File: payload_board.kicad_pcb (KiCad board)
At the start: 4 copper layers, 100 x 100 mm, 100 parts, among them IC1 RP2040_QFN56, IC2 AZ1117CH-3.3TRG1, J1 Cam_PicoLock, J12 5025700893, J12 FC Breakout, J15 SWC, J2 Cam_Conn, J3 Antenna_Conn, J4 usb jumper, J5 Display_Conn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

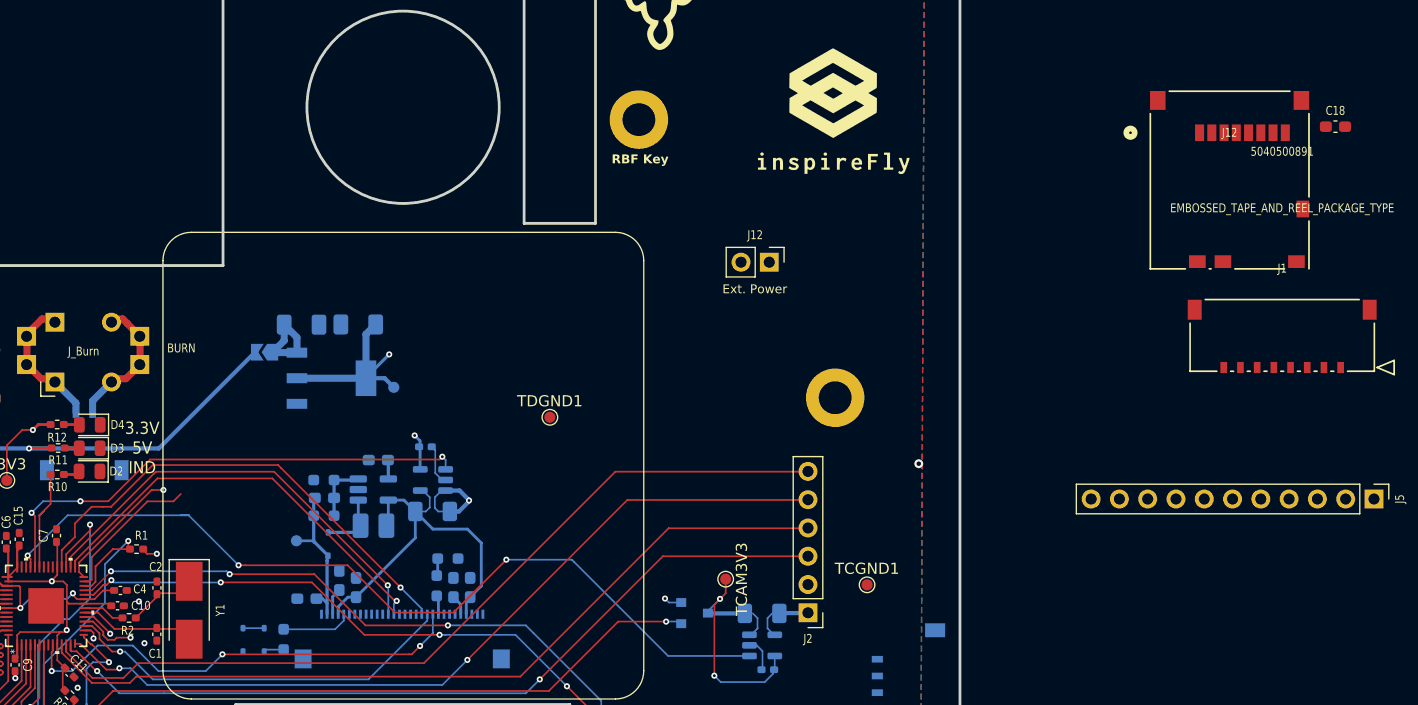
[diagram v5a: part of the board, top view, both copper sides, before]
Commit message: Moved the sd card on the board
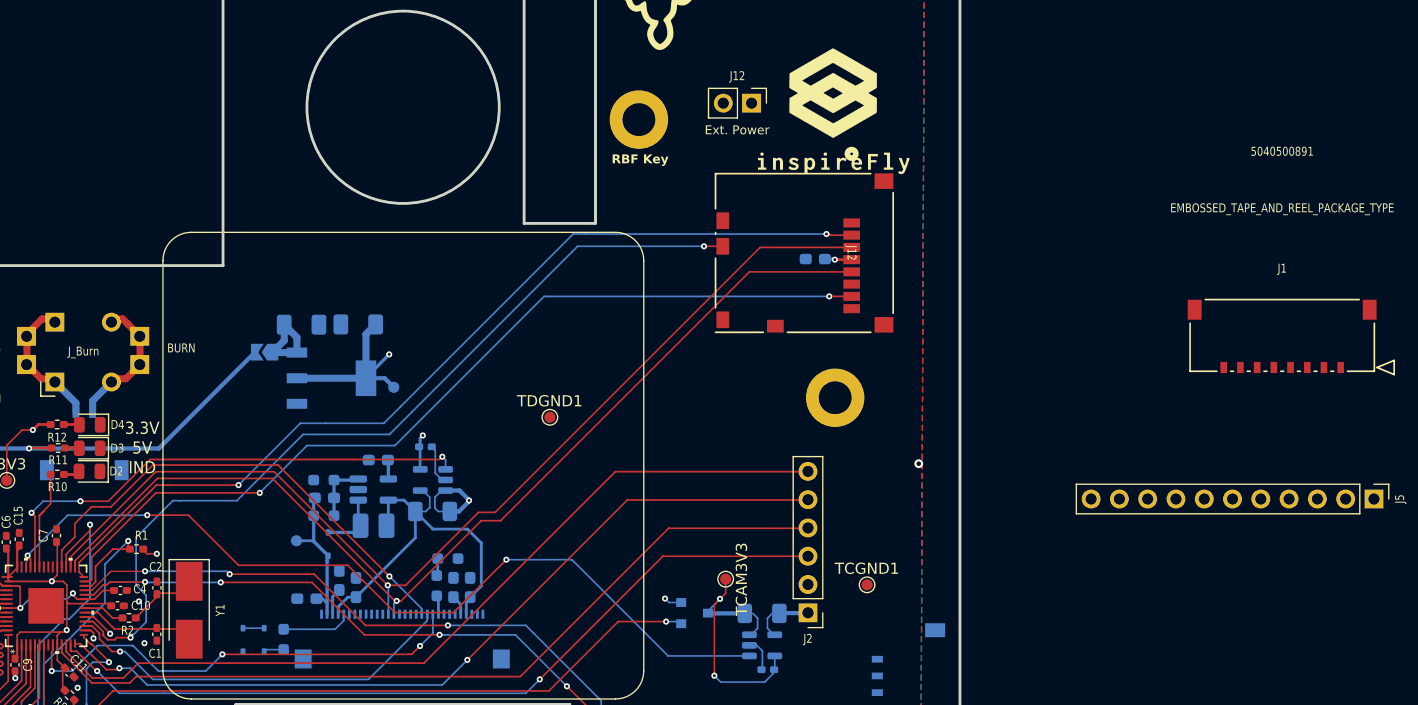
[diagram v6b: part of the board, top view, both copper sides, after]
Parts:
- C18: moved to B.Cu
- moved C18 48.2 mm to (100.0, 50.5), turned to 180 degrees
- moved J12 38.8 mm to (99.0, 50.0), turned to -90 degrees
- moved J12 14.4 mm to (94.3, 36.5)
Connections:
- J12 pad 11: (no net) -> GND
- J12 pad 12: (no net) -> GND
- J12 pad 14: (no net) -> GND
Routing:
- net SD_IND: track 5.12 -> 78.6 mm, vias 1 -> 2
- net SPI0_CS_SD: track 11.9 -> 83.1 mm, vias 1 -> 2
- net SPI0_MISO: track 13.1 -> 80.7 mm, vias 0 -> 2
- net SPI0_MOSI: track 39.5 -> 93.7 mm
- net SPI0_SCK: track 38.5 -> 91.6 mm
- net +3.3V: track 95.4 -> 97.7 mm, vias 12 -> 13
- net ADC1: track 77.5 -> 76.7 mm

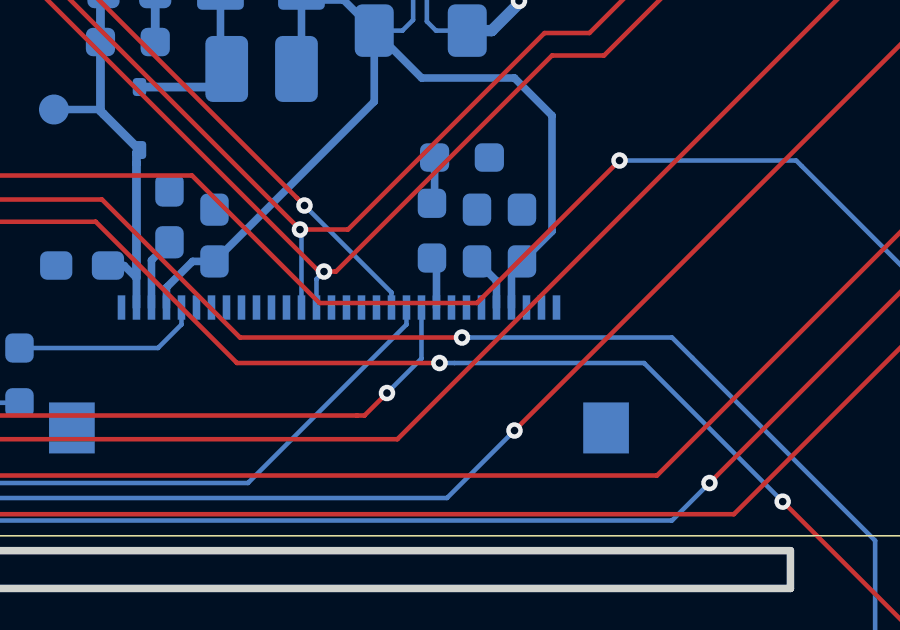
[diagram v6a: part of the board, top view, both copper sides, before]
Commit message: oops, forgot to connect some of the gnd pins
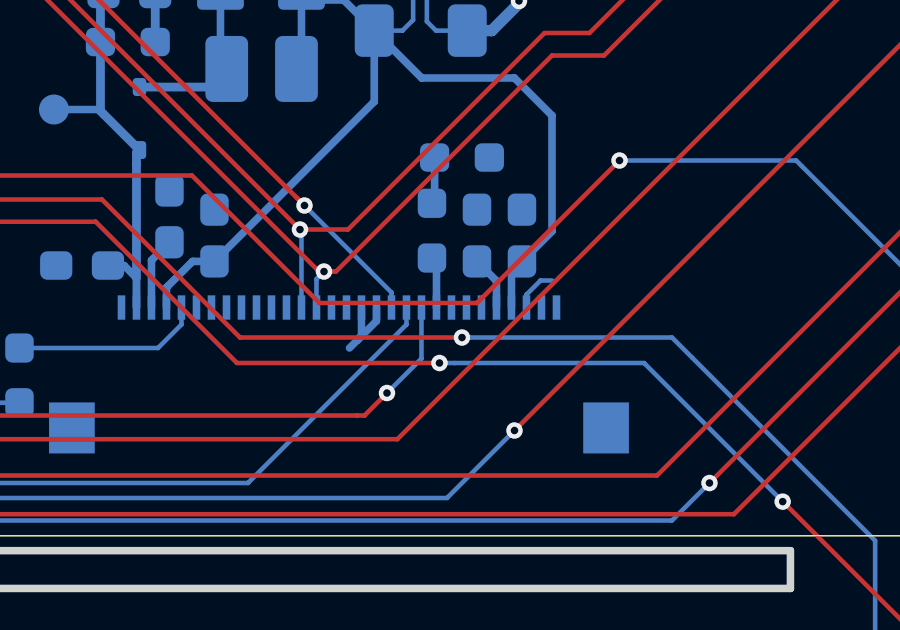
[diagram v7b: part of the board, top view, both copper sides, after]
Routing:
- net GND: track 12.0 -> 16.4 mm
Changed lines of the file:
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@@
+	)
+	(segment
+		(start 63.650001 83.349999)
+		(end 63.5 83.5)
+		(width 0.25)
+		(layer "B.Cu")
+		(net 1)
+	)
+	(segment
+		(start 69.15 82.4)
+		(end 69.15 81.969628)
+		(width 0.1524)
+		(layer "B.Cu")
+		(net 1)
 	)
 	(segment
@@
 		(start 66.488042 70.340196)
 		(end 65.8648 69.716954)
+		(width 0.1524)
+		(layer "B.Cu")
+		(net 1)
+	)
+	(segment
+		(start 64.15 82.85)
+		(end 63.5 83.5)
+		(width 0.25)
+		(layer "B.Cu")
+		(net 1)
+	)
+	(segment
+		(start 69.619628 81.5)
+		(end 70 81.5)
+		(width 0.1524)
+		(layer "B.Cu")
+		(net 1)
+	)
+	(segment
+		(start 63.5 83.5)
+		(end 63.25 83.75)
+		(width 0.25)
+		(layer "B.Cu")
+		(net 1)
+	)
+	(segment
+		(start 63.650001 82.4)
+		(end 63.650001 83.349999)
+		(width 0.25)
+		(layer "B.Cu")
+		(net 1)
+	)
+	(segment
+		(start 69.15 81.969628)
+		(end 69.619628 81.5)
 		(width 0.1524)
 		(layer "B.Cu")
@@
 		(layer "B.Cu")
 		(net 1)
+	)
+	(segment
+		(start 64.15 82.4)
+		(end 64.15 82.85)
+		(width 0.25)
+		(layer "B.Cu")
+		(net 1)

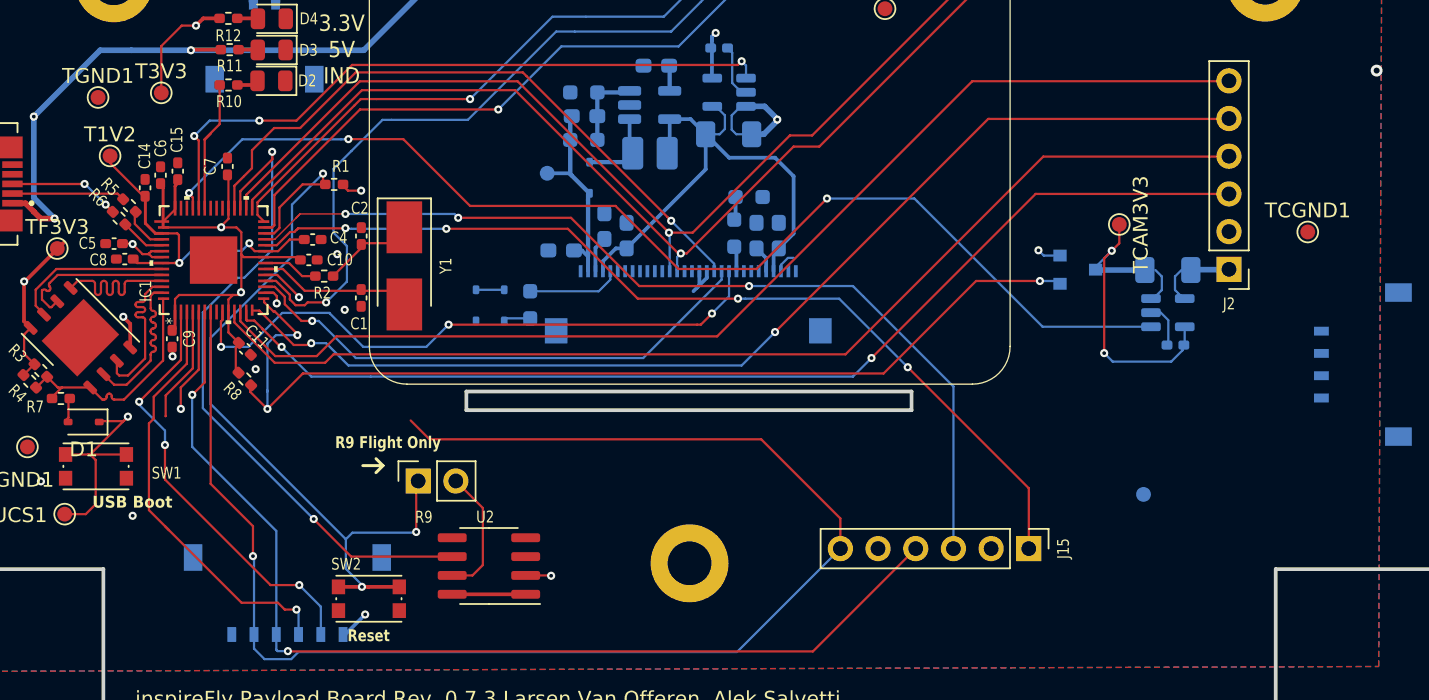
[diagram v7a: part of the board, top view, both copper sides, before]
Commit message: Some of the planes where unconnected
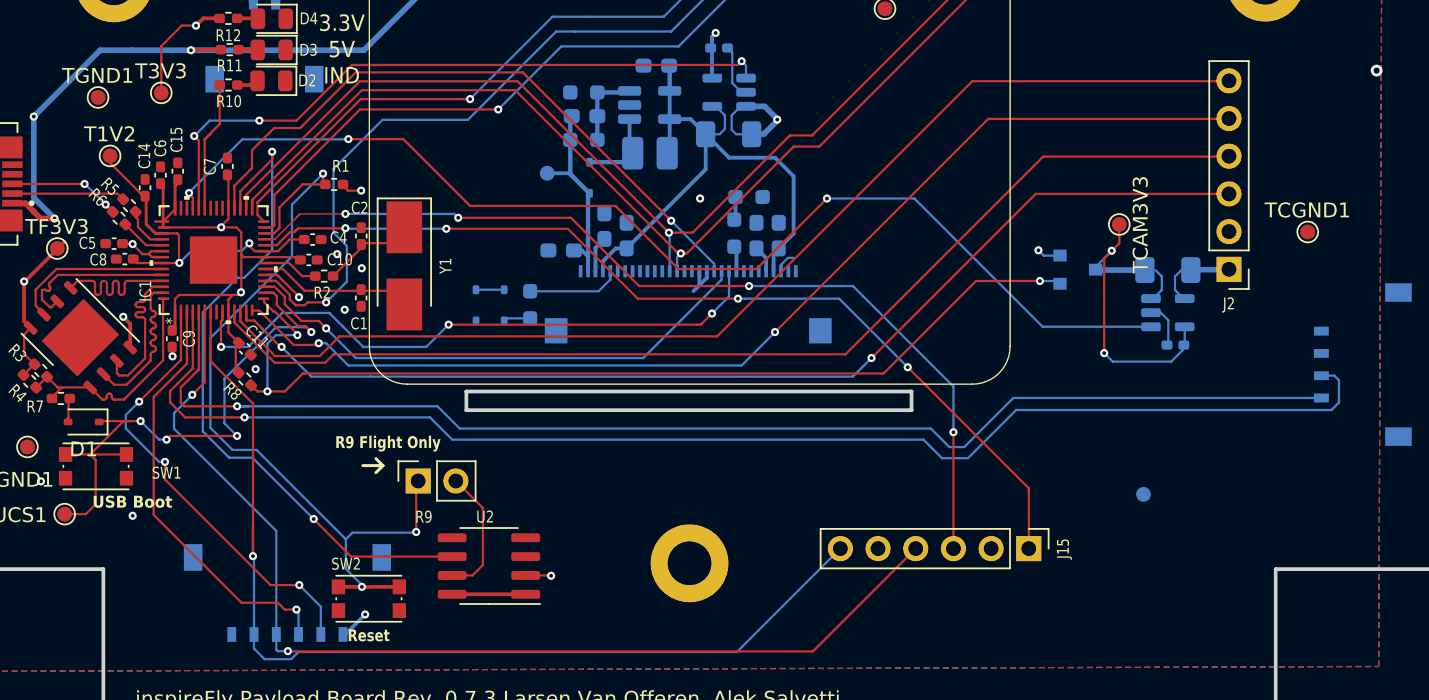
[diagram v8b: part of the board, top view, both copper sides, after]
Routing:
- net I2C1_SDA: track 7.88 -> 91.5 mm, vias 0 -> 1
- net I2C1_SCL: track 7.13 -> 86.7 mm
- net UART1_RX: track 100.6 -> 68.9 mm
- net /USBBOOT: track 17.0 -> 39.8 mm, vias 2 -> 4
- net Cam_RST: track 69.4 -> 66.8 mm
- net DIN-: track 36.9 -> 38.8 mm
- net UART1_TX: track 71.6 -> 72.6 mm
- net Break_SDA: track 29.2 -> 30.2 mm
- net /~{RESET}: track 55.0 -> 55.9 mm
- net WDT_WDI: track 45.2 -> 46.1 mm
- net Break_SCL: track 29.3 -> 28.7 mm
- net SWDIO: vias 3 -> 4
- net GND: vias 9 -> 11
